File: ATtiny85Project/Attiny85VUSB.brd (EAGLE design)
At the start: 50 x 50 mm, 30 parts

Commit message: Small fixes to attiny85 to use other pins
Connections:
- net N$1 renamed DMIN
- net N$4 renamed DPLUS
- net PB1: now also IC1.2; no longer IC1.6
- net PB2: now also IC1.3; no longer IC1.7
- net PB3: no longer IC1.2
- net PB4: no longer IC1.3
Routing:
- net GND: track 18.1 -> 0.00 mm
- net PB1: track 18.8 -> 36.2 mm, vias 0 -> 1
- net PB2: track 22.6 -> 29.0 mm, vias 0 -> 1
- net PB4: track 15.5 -> 9.42 mm
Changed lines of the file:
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@@
 <?xml version="1.0" encoding="utf-8"?>
 <!DOCTYPE eagle SYSTEM "eagle.dtd">
-<eagle version="6.5.0">
+<eagle version="7.5.0">
 <drawing>
 <settings>
@@
 <layer number="59" name="tCarbon" color="7" fill="1" visible="no" active="no"/>
 <layer number="60" name="bCarbon" color="7" fill="1" visible="no" active="no"/>
-<layer number="90" name="Modules" color="5" fill="1" visible="yes" active="yes"/>
+<layer number="90" name="Modules" color="5" fill="1" visible="no" active="no"/>
 <layer number="91" name="Nets" color="2" fill="1" visible="no" active="no"/>
 <layer number="92" name="Busses" color="1" fill="1" visible="no" active="no"/>
@@
 <pass name="Default">
 <param name="RoutingGrid" value="50mil"/>
+<param name="AutoGrid" value="1"/>
+<param name="Efforts" value="0"/>
+<param name="TopRouterVariant" value="1"/>
 <param name="tpViaShape" value="round"/>
 <param name="PrefDir.1" value="|"/>
@@
 <signals>
 <signal name="PB1">
-<contactref element="IC1" pad="6"/>
 <contactref element="R1" pad="2"/>
 <contactref element="JP3" pad="3"/>
-<wire x1="33.02" y1="10.16" x2="33.02" y2="2.54" width="0.3048" layer="1"/>
-<wire x1="33.02" y1="10.16" x2="33.02" y2="8.89" width="0.3048" layer="16"/>
 <wire x1="33.02" y1="8.89" x2="31.75" y2="7.62" width="0.3048" layer="16"/>
 <wire x1="31.75" y1="7.62" x2="23.622" y2="7.62" width="0.3048" layer="16"/>
+<contactref element="IC1" pad="2"/>
+<wire x1="33.02" y1="8.89" x2="33.02" y2="10.16" width="0.4064" layer="16"/>
+<via x="33.02" y="10.16" extent="1-16" drill="0.6" shape="square"/>
+<wire x1="33.02" y1="2.54" x2="33.02" y2="10.16" width="0.4064" layer="1"/>
+<wire x1="33.02" y1="10.16" x2="33.02" y2="15.24" width="0.4064" layer="1"/>
+<wire x1="33.02" y1="15.24" x2="31.75" y2="16.51" width="0.4064" layer="1"/>
+<wire x1="31.75" y1="16.51" x2="31.75" y2="20.32" width="0.4064" layer="1"/>
+<wire x1="31.75" y1="20.32" x2="33.02" y2="21.59" width="0.4064" layer="1"/>
+<wire x1="33.02" y1="21.59" x2="34.29" y2="20.32" width="0.4064" layer="1"/>
+<wire x1="34.29" y1="20.32" x2="34.29" y2="19.05" width="0.4064" layer="1"/>
+<wire x1="34.29" y1="19.05" x2="35.56" y2="17.78" width="0.4064" layer="1"/>
 </signal>
 <signal name="PB2">
-<contactref element="IC1" pad="7"/>
 <contactref element="R2" pad="2"/>
 <contactref element="JP3" pad="2"/>
-<wire x1="35.56" y1="10.16" x2="35.56" y2="2.54" width="0.3048" layer="1"/>
-<wire x1="35.56" y1="10.16" x2="35.56" y2="8.89" width="0.3048" layer="16"/>
 <wire x1="35.56" y1="8.89" x2="31.75" y2="6.35" width="0.3048" layer="16"/>
 <wire x1="31.75" y1="6.35" x2="26.162" y2="6.35" width="0.3048" layer="16"/>
 <wire x1="26.162" y1="6.35" x2="23.622" y2="3.81" width="0.3048" layer="16"/>
-</signal>
-<signal name="N$4">
+<contactref element="IC1" pad="3"/>
+<wire x1="33.02" y1="17.78" x2="33.02" y2="16.51" width="0.4064" layer="1"/>
+<wire x1="33.02" y1="16.51" x2="36.83" y2="13.97" width="0.4064" layer="1"/>
+<wire x1="36.83" y1="13.97" x2="40.64" y2="13.97" width="0.4064" layer="1"/>
+<wire x1="35.56" y1="8.89" x2="35.56" y2="10.16" width="0.4064" layer="16"/>
+<via x="35.56" y="10.16" extent="1-16" drill="0.6" shape="square"/>
+<wire x1="35.56" y1="10.16" x2="35.56" y2="12.7" width="0.4064" layer="1"/>
+<wire x1="35.56" y1="12.7" x2="36.83" y2="13.97" width="0.4064" layer="1"/>
+<wire x1="31.75" y1="6.35" x2="35.56" y2="2.54" width="0" layer="19" extent="16-16"/>
+</signal>
+<signal name="DPLUS">
 <contactref element="R2" pad="1"/>
 <contactref element="D1" pad="C"/>
@@
 <wire x1="12.7" y1="3.81" x2="14.478" y2="3.81" width="0.4064" layer="16"/>
 </signal>
-<signal name="N$1">
+<signal name="DMIN">
 <contactref element="R1" pad="1"/>
 <contactref element="R3" pad="1"/>
@@
 <contactref element="JP2" pad="1"/>
 <contactref element="JP2" pad="2"/>
-<wire x1="30.48" y1="17.78" x2="30.48" y2="16.51" width="0.3048" layer="1"/>
-<wire x1="30.48" y1="16.51" x2="34.29" y2="12.7" width="0.3048" layer="1"/>
-<wire x1="34.29" y1="12.7" x2="45.72" y2="12.7" width="0.3048" layer="1"/>
 <polygon width="0.4064" layer="1">
 <vertex x="0" y="0"/>
@@
 </signal>
 <signal name="PB3">
-<contactref element="IC1" pad="2"/>
 <contactref element="PB3" pad="A"/>
 <contactref element="JP4" pad="2"/>
 <wire x1="39.37" y1="15.24" x2="41.91" y2="17.78" width="0.3048" layer="1"/>
 <wire x1="41.91" y1="17.78" x2="45.72" y2="17.78" width="0.3048" layer="1"/>
-<wire x1="35.56" y1="17.78" x2="35.56" y2="16.51" width="0.3048" layer="1"/>
 <wire x1="35.56" y1="16.51" x2="36.83" y2="15.24" width="0.3048" layer="1"/>
 <wire x1="36.83" y1="15.24" x2="39.37" y2="15.24" width="0.3048" layer="1"/>
-<wire x1="35.56" y1="17.78" x2="35.56" y2="20.32" width="0.3048" layer="1"/>
 <wire x1="35.56" y1="20.32" x2="29.21" y2="26.67" width="0.3048" layer="1"/>
 <wire x1="29.21" y1="36.83" x2="29.21" y2="26.67" width="0.3048" layer="1"/>
+<wire x1="35.56" y1="20.32" x2="35.56" y2="16.51" width="0.4064" layer="1"/>
 </signal>
 <signal name="PB4">
-<contactref element="IC1" pad="3"/>
 <contactref element="JP4" pad="3"/>
-<wire x1="33.02" y1="17.78" x2="33.02" y2="16.51" width="0.3048" layer="1"/>
-<wire x1="33.02" y1="16.51" x2="35.56" y2="13.97" width="0.3048" layer="1"/>
-<wire x1="35.56" y1="13.97" x2="40.64" y2="13.97" width="0.3048" layer="1"/>
 <wire x1="40.64" y1="13.97" x2="41.91" y2="15.24" width="0.3048" layer="1"/>
 <wire x1="41.91" y1="15.24" x2="45.72" y2="15.24" width="0.3048" layer="1"/>
+<wire x1="36.83" y1="13.97" x2="40.64" y2="13.97" width="0.4064" layer="1"/>
 </signal>
 <signal name="N$2">

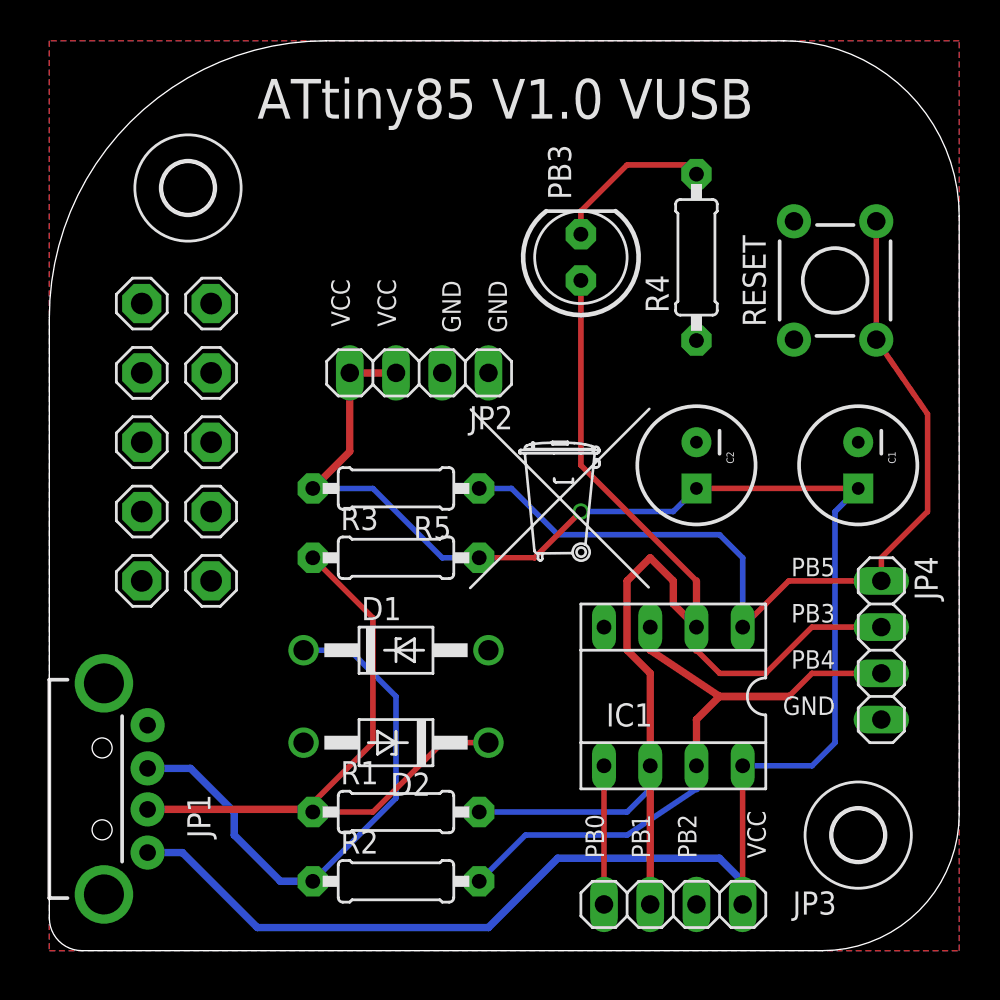
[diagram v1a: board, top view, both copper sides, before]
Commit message: Rewire ATtiny85 board to make it compatible with triket
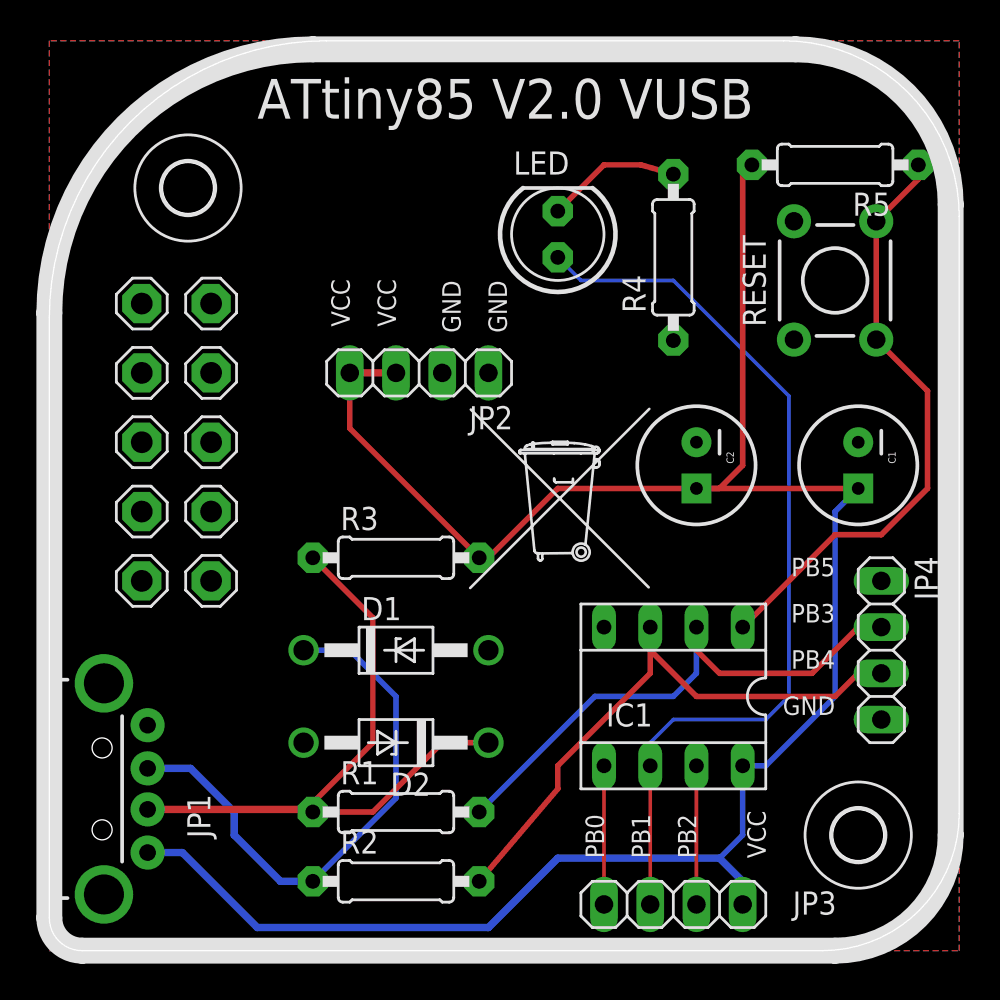
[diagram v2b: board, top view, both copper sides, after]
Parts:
- removed PB3: (no value), adafruit:LED5MM
- added LED: (no value), adafruit:LED5MM
- moved R5 30.0 mm to (43.2, 43.2)
- moved R4 1.27 mm to (34.3, 38.1)
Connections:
- new net RESET: IC1.1, R5.1, RESET.3, RESET.4
- net N$2: now also LED.K; no longer PB3.K
- net PB1: now also IC1.6, LED.A; no longer IC1.2, R1.2
- net PB2: now also IC1.7; no longer IC1.3, R2.2
- net PB3: now also IC1.2, R1.2; no longer PB3.A
- net PB4: now also IC1.3, R2.2
- net PB5: no longer IC1.1, R5.1, RESET.3, RESET.4
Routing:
- net PB5: track 50.2 -> 0.00 mm
- net RESET: track 0.00 -> 33.2 mm
- net PB4: track 9.42 -> 33.2 mm
- net PB2: track 29.0 -> 7.62 mm, vias 1 -> 0
- net PB1: track 36.2 -> 49.9 mm, vias 1 -> 0
- net VCC: track 108.4 -> 119.8 mm, vias 1 -> 0
- net PB3: track 34.7 -> 30.6 mm
- net N$2: track 8.88 -> 7.47 mm
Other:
- board text added: "ATtiny85 V2.0 VUSB"
- board text removed: "ATtiny85 V1.0 VUSB"

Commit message: Testing for V2 of the board, sent to fab
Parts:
- added U$5: (no value), atmel:LOGO
- moved U$2 20.3 mm to (40.6, 36.8)
- moved U$1 1.27 mm to (27.9, 21.6)
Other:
- board text added: "Hardware Hacker"
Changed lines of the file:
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@@
 <wire x1="13.73715" y1="49.53" x2="42.12469375" y2="49.53" width="1.4224" layer="22"/>
 <wire x1="42.12469375" y1="49.53" x2="49.53" y2="42.12469375" width="1.4224" layer="22" curve="-90"/>
+<text x="26.67" y="44.45" size="2.032" layer="1" font="vector" rot="R180">Hardware
+Hacker</text>
 </plain>
 <attributes>
@@
 <element name="C2" library="SparkFun-Capacitors" package="CPOL-RADIAL-100UF-25V" value="0.1uF" x="35.56" y="26.67" rot="R270"/>
 <element name="LED" library="adafruit" package="LED5MM" value="" x="27.94" y="39.37" smashed="yes" rot="R90">
-<attribute name="NAME" x="28.575" y="43.9166" size="1.27" layer="25" ratio="10" rot="R180"/>
+<attribute name="NAME" x="31.115" y="43.9166" size="1.27" layer="25" ratio="10" rot="R180"/>
 <attribute name="VALUE" x="29.7434" y="42.5704" size="1.27" layer="27" ratio="10" rot="R90"/>
 </element>
@@
 </element>
 <element name="LSP6" library="solpad" package="MCS08" value="MCS08" x="5.08" y="24.13" smashed="yes">
-<attribute name="VALUE" x="5.08" y="24.511" size="0.0254" layer="27"/>
+<attribute name="VALUE" x="6.35" y="25.781" size="0.0254" layer="27"/>
 </element>
 <element name="LSP7" library="solpad" package="MCS08" value="MCS08" x="8.89" y="24.13" smashed="yes">
@@
 <attribute name="VALUE" x="5.08" y="20.701" size="0.0254" layer="27"/>
 </element>
-<element name="U$1" library="logo" package="TONNE_10.00" value="" x="27.94" y="22.86"/>
-<element name="U$2" library="logo" package="TONNE_10.00" value="" x="20.32" y="36.83" rot="MR0"/>
+<element name="U$1" library="logo" package="TONNE_10.00" value="" x="27.94" y="21.59"/>
+<element name="U$2" library="logo" package="TONNE_10.00" value="" x="40.64" y="36.83" rot="MR0"/>
 <element name="U$3" library="holes" package="2,8" value="" x="44.45" y="6.35"/>
 <element name="U$4" library="holes" package="2,8" value="" x="7.62" y="41.91"/>
+<element name="U$5" library="atmel" package="LOGO" value="" x="29.21" y="10.16" rot="R90"/>
 </elements>
 <signals>
@@
 </board>
 </drawing>
+<compatibility>
+<note version="6.3" minversion="6.2.2" severity="warning">
+Since Version 6.2.2 text objects can contain more than one line,
+which will not be processed correctly with this version.
+</note>
+</compatibility>
 </eagle>
